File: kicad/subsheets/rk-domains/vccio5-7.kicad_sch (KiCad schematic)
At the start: 7 parts, among them U5 RK3566

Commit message: Mark as R1.0
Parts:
- renumbered C130 to C74, C126 to C75, C136 to C76, C153 to C77, C154 to C78, R45 to R31
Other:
- company: (none) -> UVic Rocketry
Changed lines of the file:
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@@
 	(title_block
 		(title "VCCIO 5/6/7")
+		(date "2025-11-23")
+		(rev "1.0")
+		(company "UVic Rocketry")
+		(comment 1 "Author: Eric Handley")
 	)
 	(text "I2C2"
@@
 		(dnp no)
 		(fields_autoplaced yes)
-		(property "Reference" "#PWR088"
+		(property "Reference" "#PWR058"
 			(at 182.88 146.05 0)
 			(effects
@@
 			(project "srad-camera"
 				(path "/da62c771-e8c9-451f-8df1-ec995aadcb11/279fc251-45a8-41a3-8fcf-5855d7fe07da/bc57332b-40b9-4ce4-9f21-5e9cd84ef305"
-					(reference "#PWR088")
+					(reference "#PWR058")
 					(unit 1)
 				)
@@
 		(on_board yes)
 		(dnp no)
-		(property "Reference" "C136"
+		(property "Reference" "C76"
 			(at 184.658 109.474 0)
 			(effects
@@
 			(project "srad-camera"
 				(path "/da62c771-e8c9-451f-8df1-ec995aadcb11/279fc251-45a8-41a3-8fcf-5855d7fe07da/bc57332b-40b9-4ce4-9f21-5e9cd84ef305"
-					(reference "C136")
+					(reference "C76")
 					(unit 1)
 				)
@@
 		(on_board yes)
 		(dnp no)
-		(property "Reference" "C153"
+		(property "Reference" "C77"
 			(at 180.848 133.604 0)
 			(effects
@@
 			(project "srad-camera"
 				(path "/da62c771-e8c9-451f-8df1-ec995aadcb11/279fc251-45a8-41a3-8fcf-5855d7fe07da/bc57332b-40b9-4ce4-9f21-5e9cd84ef305"
-					(reference "C153")
+					(reference "C77")
 					(unit 1)
 				)
@@
 		(on_board yes)
 		(dnp no)
-		(property "Reference" "C154"
+		(property "Reference" "C78"
 			(at 189.992 133.604 0)
 			(effects
@@
 			(project "srad-camera"
 				(path "/da62c771-e8c9-451f-8df1-ec995aadcb11/279fc251-45a8-41a3-8fcf-5855d7fe07da/bc57332b-40b9-4ce4-9f21-5e9cd84ef305"
-					(reference "C154")
+					(reference "C78")
 					(unit 1)
 				)
@@
 		(dnp no)
 		(fields_autoplaced yes)
-		(property "Reference" "#PWR070"
+		(property "Reference" "#PWR056"
 			(at 114.3 91.44 0)
 			(effects
@@
 			(project "srad-camera"
 				(path "/da62c771-e8c9-451f-8df1-ec995aadcb11/279fc251-45a8-41a3-8fcf-5855d7fe07da/bc57332b-40b9-4ce4-9f21-5e9cd84ef305"
-					(reference "#PWR070")
+					(reference "#PWR056")
 					(unit 1)
 				)
@@
 		(on_board yes)
 		(dnp no)
-		(property "Reference" "#PWR066"
+		(property "Reference" "#PWR057"
 			(at 191.77 104.14 0)
 			(effects
@@
 			(project "srad-camera"
 				(path "/da62c771-e8c9-451f-8df1-ec995aadcb11/279fc251-45a8-41a3-8fcf-5855d7fe07da/bc57332b-40b9-4ce4-9f21-5e9cd84ef305"
-					(reference "#PWR066")
+					(reference "#PWR057")
 					(unit 1)
 				)
@@
 		(on_board yes)
 		(dnp no)
-		(property "Reference" "R45"
+		(property "Reference" "R31"
 			(at 195.072 122.174 0)
 			(effects
@@
 			(project "srad-camera"
 				(path "/da62c771-e8c9-451f-8df1-ec995aadcb11/279fc251-45a8-41a3-8fcf-5855d7fe07da/bc57332b-40b9-4ce4-9f21-5e9cd84ef305"
-					(reference "R45")
+					(reference "R31")
 					(unit 1)
 				)
@@
 		(on_board yes)
 		(dnp no)
-		(property "Reference" "C126"
+		(property "Reference" "C75"
 			(at 184.912 96.774 0)
 			(effects
@@
 			(project "srad-camera"
 				(path "/da62c771-e8c9-451f-8df1-ec995aadcb11/279fc251-45a8-41a3-8fcf-5855d7fe07da/bc57332b-40b9-4ce4-9f21-5e9cd84ef305"
-					(reference "C126")
+					(reference "C75")
 					(unit 1)
 				)
@@
 		(dnp no)
 		(fields_autoplaced yes)
-		(property "Reference" "C130"
+		(property "Reference" "C74"
 			(at 112.268 82.3025 0)
 			(effects
@@
 			(project "srad-camera"
 				(path "/da62c771-e8c9-451f-8df1-ec995aadcb11/279fc251-45a8-41a3-8fcf-5855d7fe07da/bc57332b-40b9-4ce4-9f21-5e9cd84ef305"
-					(reference "C130")
+					(reference "C74")
 					(unit 1)
 				)

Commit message: Annotations
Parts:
- renumbered C74 to C87, C75 to C88, C76 to C89, C77 to C90, C78 to C91, R31 to R34
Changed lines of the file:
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@@
 		(dnp no)
 		(fields_autoplaced yes)
-		(property "Reference" "#PWR058"
+		(property "Reference" "#PWR068"
 			(at 182.88 146.05 0)
 			(effects
@@
 			(project "srad-camera"
 				(path "/da62c771-e8c9-451f-8df1-ec995aadcb11/279fc251-45a8-41a3-8fcf-5855d7fe07da/bc57332b-40b9-4ce4-9f21-5e9cd84ef305"
-					(reference "#PWR058")
+					(reference "#PWR068")
 					(unit 1)
 				)
@@
 		(on_board yes)
 		(dnp no)
-		(property "Reference" "C76"
+		(property "Reference" "C89"
 			(at 184.658 109.474 0)
 			(effects
@@
 			(project "srad-camera"
 				(path "/da62c771-e8c9-451f-8df1-ec995aadcb11/279fc251-45a8-41a3-8fcf-5855d7fe07da/bc57332b-40b9-4ce4-9f21-5e9cd84ef305"
-					(reference "C76")
+					(reference "C89")
 					(unit 1)
 				)
@@
 		(on_board yes)
 		(dnp no)
-		(property "Reference" "C77"
+		(property "Reference" "C90"
 			(at 180.848 133.604 0)
 			(effects
@@
 			(project "srad-camera"
 				(path "/da62c771-e8c9-451f-8df1-ec995aadcb11/279fc251-45a8-41a3-8fcf-5855d7fe07da/bc57332b-40b9-4ce4-9f21-5e9cd84ef305"
-					(reference "C77")
+					(reference "C90")
 					(unit 1)
 				)
@@
 		(on_board yes)
 		(dnp no)
-		(property "Reference" "C78"
+		(property "Reference" "C91"
 			(at 189.992 133.604 0)
 			(effects
@@
 			(project "srad-camera"
 				(path "/da62c771-e8c9-451f-8df1-ec995aadcb11/279fc251-45a8-41a3-8fcf-5855d7fe07da/bc57332b-40b9-4ce4-9f21-5e9cd84ef305"
-					(reference "C78")
+					(reference "C91")
 					(unit 1)
 				)
@@
 		(dnp no)
 		(fields_autoplaced yes)
-		(property "Reference" "#PWR056"
+		(property "Reference" "#PWR066"
 			(at 114.3 91.44 0)
 			(effects
@@
 			(project "srad-camera"
 				(path "/da62c771-e8c9-451f-8df1-ec995aadcb11/279fc251-45a8-41a3-8fcf-5855d7fe07da/bc57332b-40b9-4ce4-9f21-5e9cd84ef305"
-					(reference "#PWR056")
+					(reference "#PWR066")
 					(unit 1)
 				)
@@
 		(on_board yes)
 		(dnp no)
-		(property "Reference" "#PWR057"
+		(property "Reference" "#PWR067"
 			(at 191.77 104.14 0)
 			(effects
@@
 			(project "srad-camera"
 				(path "/da62c771-e8c9-451f-8df1-ec995aadcb11/279fc251-45a8-41a3-8fcf-5855d7fe07da/bc57332b-40b9-4ce4-9f21-5e9cd84ef305"
-					(reference "#PWR057")
+					(reference "#PWR067")
 					(unit 1)
 				)
@@
 		(on_board yes)
 		(dnp no)
-		(property "Reference" "R31"
+		(property "Reference" "R34"
 			(at 195.072 122.174 0)
 			(effects
@@
 			(project "srad-camera"
 				(path "/da62c771-e8c9-451f-8df1-ec995aadcb11/279fc251-45a8-41a3-8fcf-5855d7fe07da/bc57332b-40b9-4ce4-9f21-5e9cd84ef305"
-					(reference "R31")
+					(reference "R34")
 					(unit 1)
 				)
@@
 		(on_board yes)
 		(dnp no)
-		(property "Reference" "C75"
+		(property "Reference" "C88"
 			(at 184.912 96.774 0)
 			(effects
@@
 			(project "srad-camera"
 				(path "/da62c771-e8c9-451f-8df1-ec995aadcb11/279fc251-45a8-41a3-8fcf-5855d7fe07da/bc57332b-40b9-4ce4-9f21-5e9cd84ef305"
-					(reference "C75")
+					(reference "C88")
 					(unit 1)
 				)
@@
 		(dnp no)
 		(fields_autoplaced yes)
-		(property "Reference" "C74"
+		(property "Reference" "C87"
 			(at 112.268 82.3025 0)
 			(effects
@@
 			(project "srad-camera"
 				(path "/da62c771-e8c9-451f-8df1-ec995aadcb11/279fc251-45a8-41a3-8fcf-5855d7fe07da/bc57332b-40b9-4ce4-9f21-5e9cd84ef305"
-					(reference "C74")
+					(reference "C87")
 					(unit 1)
 				)

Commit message: Start on PCB design
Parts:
- C85: renamed from C87; footprint (none) -> Capacitor_SMD:C_0402_1005Metric; LCSC PART NAME (none) -> C1525
- C86: renamed from C88; footprint (none) -> Capacitor_SMD:C_0402_1005Metric; LCSC PART NAME (none) -> C1525
- C87: renamed from C89; footprint (none) -> Capacitor_SMD:C_0402_1005Metric; LCSC PART NAME (none) -> C1525
- C88: renamed from C90; footprint (none) -> Capacitor_SMD:C_0402_1005Metric; LCSC PART NAME (none) -> C1525
- C89: renamed from C91; footprint (none) -> Capacitor_SMD:C_0402_1005Metric; LCSC PART NAME (none) -> C1523
- R35: renamed from R34; footprint (none) -> Resistor_SMD:R_0402_1005Metric; LCSC PART NAME (none) -> C25744
- U5: LCSC PART NAME RK3566 -> (none)
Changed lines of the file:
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@@
 		(on_board yes)
 		(dnp no)
-		(property "Reference" "C89"
+		(property "Reference" "C87"
 			(at 184.658 109.474 0)
 			(effects
@@
 			)
 		)
-		(property "Footprint" ""
+		(property "Footprint" "Capacitor_SMD:C_0402_1005Metric"
 			(at 182.88 110.49 0)
 			(effects
@@
 			)
 		)
-		(property "V" ""
-			(at 182.88 110.49 90)
+		(property "LCSC PART NAME" "C1525"
+			(at 182.88 110.49 0)
 			(effects
 				(font
@@
 			(project "srad-camera"
 				(path "/da62c771-e8c9-451f-8df1-ec995aadcb11/279fc251-45a8-41a3-8fcf-5855d7fe07da/bc57332b-40b9-4ce4-9f21-5e9cd84ef305"
-					(reference "C89")
+					(reference "C87")
 					(unit 1)
 				)
@@
 		(on_board yes)
 		(dnp no)
-		(property "Reference" "C90"
+		(property "Reference" "C88"
 			(at 180.848 133.604 0)
 			(effects
@@
 			)
 		)
-		(property "Footprint" ""
+		(property "Footprint" "Capacitor_SMD:C_0402_1005Metric"
 			(at 182.88 134.62 0)
 			(effects
@@
 			)
 		)
-		(property "V" ""
+		(property "LCSC PART NAME" "C1525"
 			(at 182.88 134.62 0)
 			(effects
@@
 			(project "srad-camera"
 				(path "/da62c771-e8c9-451f-8df1-ec995aadcb11/279fc251-45a8-41a3-8fcf-5855d7fe07da/bc57332b-40b9-4ce4-9f21-5e9cd84ef305"
-					(reference "C90")
+					(reference "C88")
 					(unit 1)
 				)
@@
 		(on_board yes)
 		(dnp no)
-		(property "Reference" "C91"
+		(property "Reference" "C89"
 			(at 189.992 133.604 0)
 			(effects
@@
 			)
 		)
-		(property "Footprint" ""
+		(property "Footprint" "Capacitor_SMD:C_0402_1005Metric"
 			(at 187.96 134.62 0)
 			(effects
@@
 			)
 		)
-		(property "V" ""
+		(property "LCSC PART NAME" "C1523"
 			(at 187.96 134.62 0)
 			(effects
@@
 			(project "srad-camera"
 				(path "/da62c771-e8c9-451f-8df1-ec995aadcb11/279fc251-45a8-41a3-8fcf-5855d7fe07da/bc57332b-40b9-4ce4-9f21-5e9cd84ef305"
-					(reference "C91")
+					(reference "C89")
 					(unit 1)
 				)
@@
 			)
 		)
-		(property "LCSC PART NAME" "RK3566"
+		(property "LCSC PART NAME" ""
 			(at 207.772 91.44 0)
 			(effects
@@
 		(on_board yes)
 		(dnp no)
-		(property "Reference" "R34"
+		(property "Reference" "R35"
 			(at 195.072 122.174 0)
 			(effects
@@
 			)
 		)
-		(property "Footprint" ""
+		(property "Footprint" "Resistor_SMD:R_0402_1005Metric"
 			(at 191.77 123.19 0)
 			(effects
@@
 		)
 		(property "SUPPLEMENTARY FEATURES" ""
+			(at 191.77 123.19 0)
+			(effects
+				(font
+					(size 1.27 1.27)
+				)
+				(hide yes)
+			)
+		)
+		(property "LCSC PART NAME" "C25744"
 			(at 191.77 123.19 0)
 			(effects
@@
 			(project "srad-camera"
 				(path "/da62c771-e8c9-451f-8df1-ec995aadcb11/279fc251-45a8-41a3-8fcf-5855d7fe07da/bc57332b-40b9-4ce4-9f21-5e9cd84ef305"
-					(reference "R34")
+					(reference "R35")
 					(unit 1)
 				)
@@
 		(on_board yes)
 		(dnp no)
-		(property "Reference" "C88"
+		(property "Reference" "C86"
 			(at 184.912 96.774 0)
 			(effects
@@
 			)
 		)
-		(property "Footprint" ""
+		(property "Footprint" "Capacitor_SMD:C_0402_1005Metric"
 			(at 182.88 97.79 0)
 			(effects
@@
 			)
 		)
-		(property "V" ""
-			(at 182.88 97.79 90)
+		(property "LCSC PART NAME" "C1525"
+			(at 182.88 97.79 0)
 			(effects
 				(font
@@
 			(project "srad-camera"
 				(path "/da62c771-e8c9-451f-8df1-ec995aadcb11/279fc251-45a8-41a3-8fcf-5855d7fe07da/bc57332b-40b9-4ce4-9f21-5e9cd84ef305"
-					(reference "C88")
+					(reference "C86")
 					(unit 1)
 				)
@@
 		(dnp no)
 		(fields_autoplaced yes)
-		(property "Reference" "C87"
+		(property "Reference" "C85"
 			(at 112.268 82.3025 0)
 			(effects
@@
 			)
 		)
-		(property "Footprint" ""
+		(property "Footprint" "Capacitor_SMD:C_0402_1005Metric"
 			(at 114.3 81.28 0)
 			(effects
@@
 			)
 		)
-		(property "V" ""
-			(at 114.3 81.28 90)
+		(property "LCSC PART NAME" "C1525"
+			(at 114.3 81.28 0)
 			(effects
 				(font
@@
 			(project "srad-camera"
 				(path "/da62c771-e8c9-451f-8df1-ec995aadcb11/279fc251-45a8-41a3-8fcf-5855d7fe07da/bc57332b-40b9-4ce4-9f21-5e9cd84ef305"
-					(reference "C87")
+					(reference "C85")
 					(unit 1)
 				)

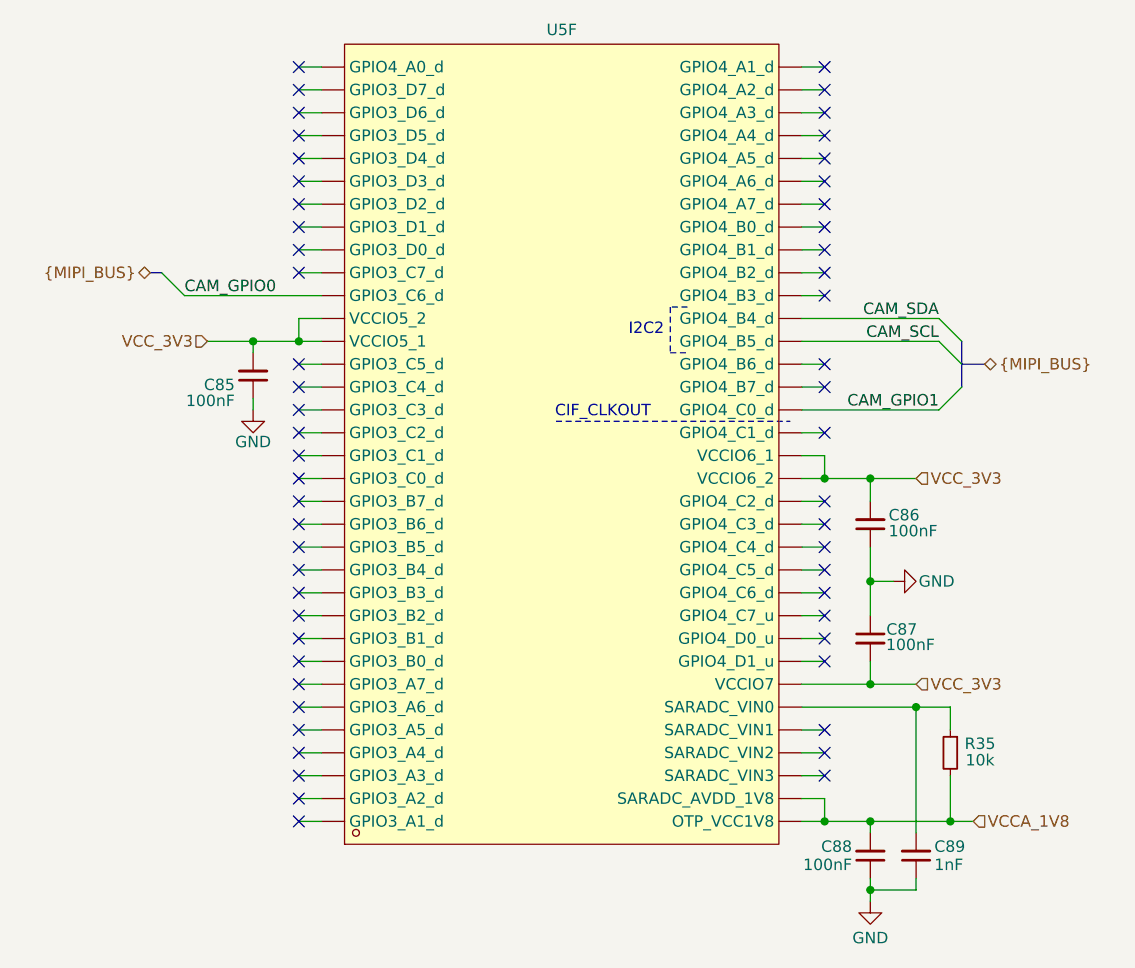
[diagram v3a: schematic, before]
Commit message: Remove power/decoupling for unused power domains
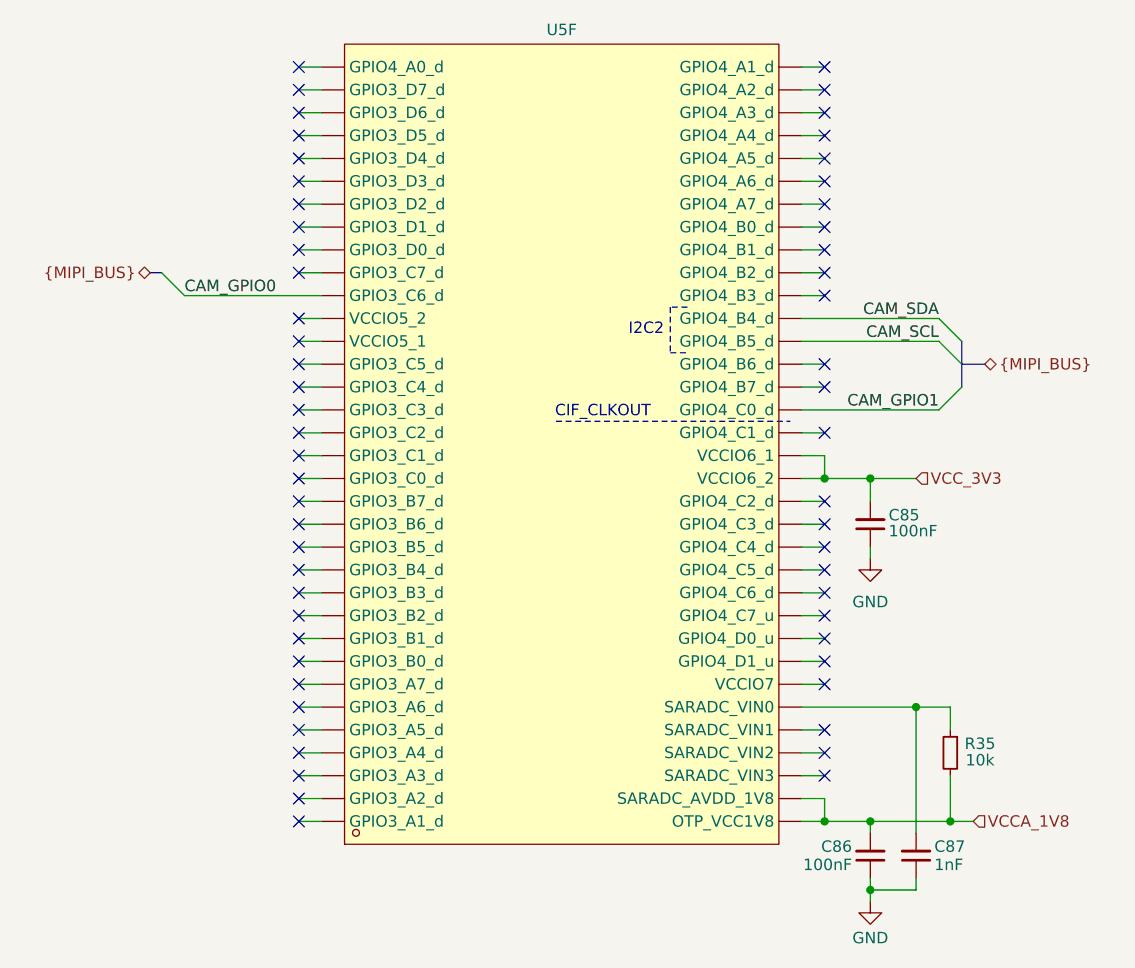
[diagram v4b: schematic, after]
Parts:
- removed C85, C87: 100nF, Capacitor_SMD:C_0402_1005Metric, symbol Device:C_Small
- renumbered C86 to C85, C88 to C86, C89 to C87
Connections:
- net VCC_3V3: no longer U5.1N5 (VCCIO5_1), U5.1N6 (VCCIO5_2), U5.1N8 (VCCIO7)
- no-connect marks 56 -> 59
